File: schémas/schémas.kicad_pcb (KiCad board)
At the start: 2 copper layers, 45 x 40.5 mm, 6 parts, among them J2 Conn_01x04, J3 Conn_01x08, J4 Conn_01x08, J5 Conn_01x03

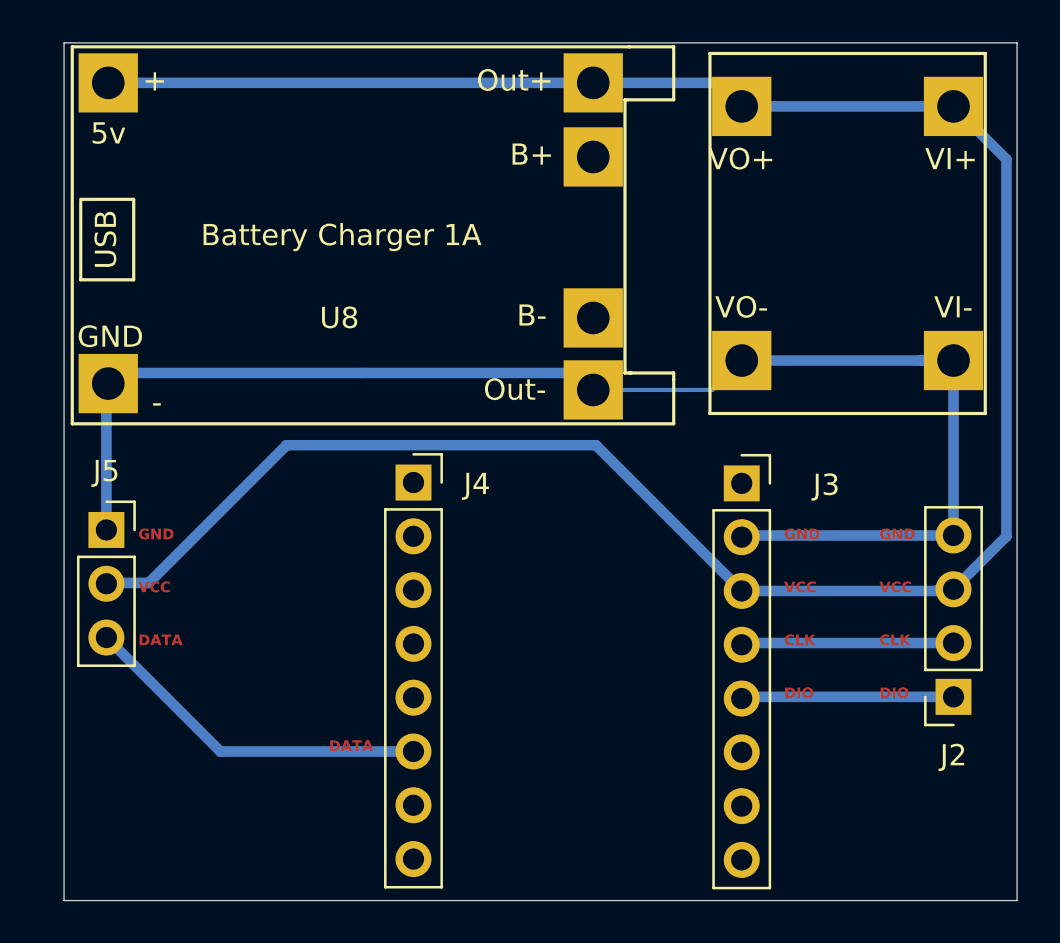
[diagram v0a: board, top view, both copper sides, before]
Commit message: feat: added button to diagram
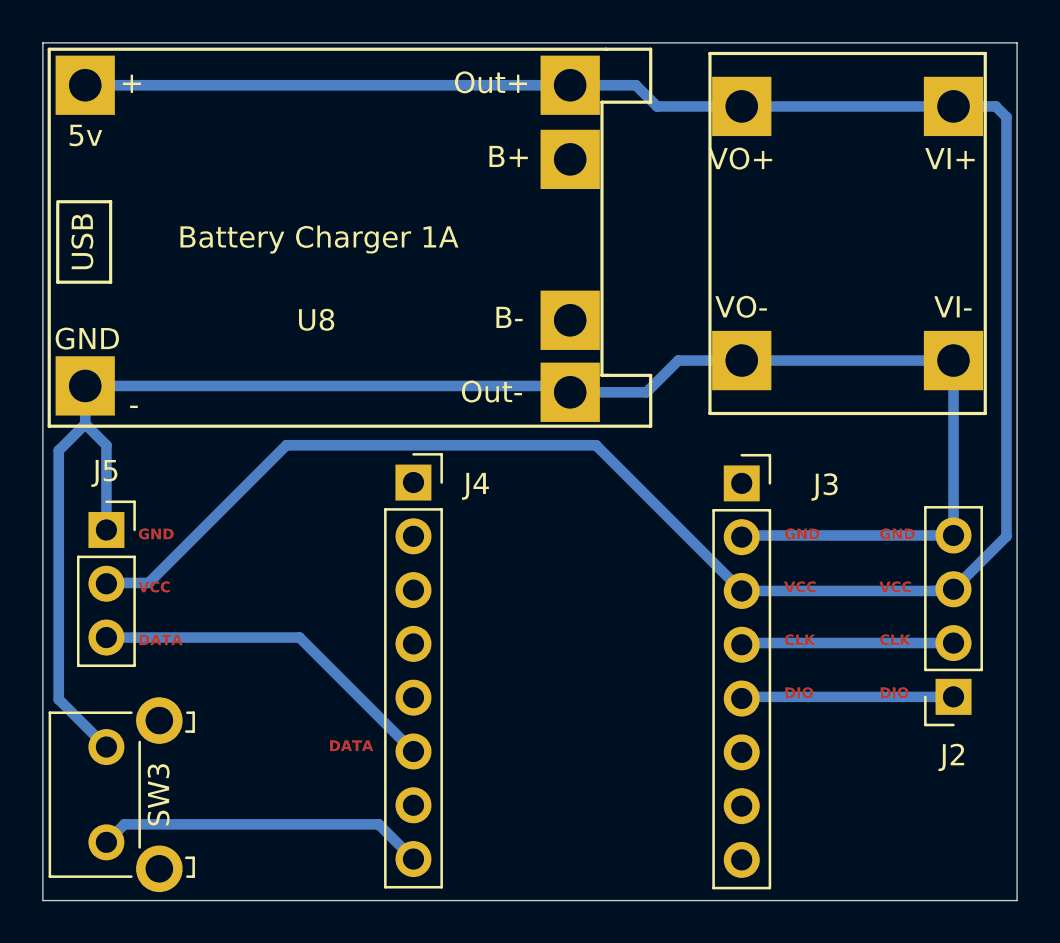
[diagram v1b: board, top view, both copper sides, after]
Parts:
- added SW3: SW_Push, Button_Switch_THT:SW_Tactile_SKHH_Angled, F.Cu at (167.5, 82.8)
- moved U8 1.09 mm to (164.8, 45.3)
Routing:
- net GND: track 67.4 -> 84.5 mm
- net Net-(J4-Pin_8): track 0.00 -> 15.5 mm
- net +3.3V: track 110.8 -> 113.0 mm
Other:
- board size 45 x 40.5 mm -> 46 x 40.5 mm

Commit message: feat: changed schemas
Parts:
- moved U9 159.1 mm to (57.6, 13.5), turned to -90 degrees
- moved U8 155.2 mm to (12.9, 13.3)
- moved J4 147.3 mm to (37.6, 36.7)
- moved J2 146.8 mm to (63.6, 46.8)
- moved J3 146.8 mm to (53.6, 36.8)
- moved J5 93.5 mm to (74.6, 57.5)
- moved SW3 83.7 mm to (91.1, 48.5), turned to -90 degrees
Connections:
- U8 pad 1: +3.3V -> unconnected-(U8-IN+-Pad1)
- U8 pad 2: GND -> unconnected-(U8-IN--Pad2)
- U8 pad 3: +3.3V -> Net-(U8-OUT+)
- U8 pad 4: GND -> Net-(U8-OUT-)
- U9 pad 1: GND -> Net-(U8-OUT-)
- U9 pad 2: +3.3V -> Net-(U8-OUT+)
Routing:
- net +3.3V: track 113.0 -> 49.5 mm
- net Net-(J4-Pin_8): track 15.5 -> 63.9 mm
- net Net-(U8-OUT-): track 0.00 -> 26.3 mm
- net Net-(J4-Pin_6): track 16.7 -> 42.4 mm
- net GND: track 84.5 -> 71.2 mm
- net Net-(U8-OUT+): track 0.00 -> 8.60 mm
- net unconnected-(U8-IN--Pad2): track 0.00 -> 1.13 mm
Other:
- board size 46 x 40.5 mm -> 81.5 x 53.5 mm
